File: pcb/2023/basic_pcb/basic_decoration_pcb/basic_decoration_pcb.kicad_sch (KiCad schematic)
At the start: 15 parts, among them J1 Conn_01x15_Socket, J2 Conn_01x15_Socket, J3 Screw_Terminal_01x03, Q1 BT136-500, U1 MOC3041M

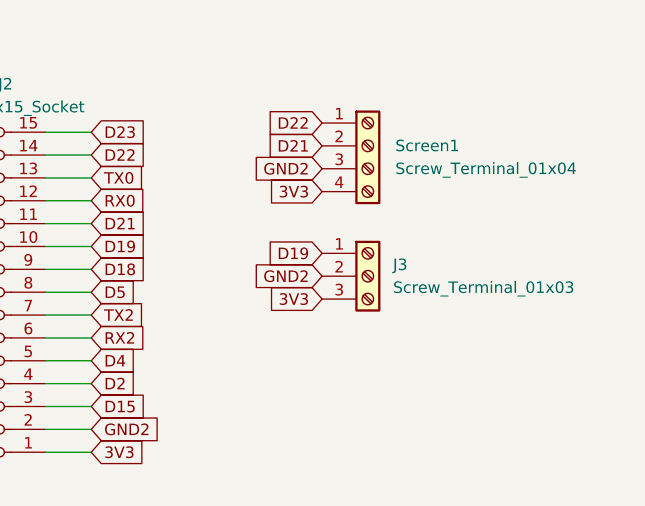
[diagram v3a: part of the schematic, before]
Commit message: update, fixed bug on the PCB, a pull up resistor is required for the DHT11 to work well, so now it's added
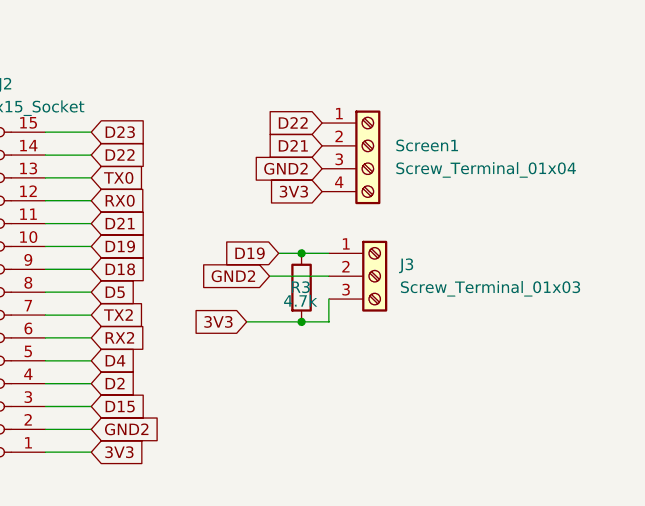
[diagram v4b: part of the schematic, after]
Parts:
- added R3: 4.7k_0603, Resistor_THT:R_Axial_DIN0204_L3.6mm_D1.6mm_P7.62mm_Horizontal, symbol PCM_4ms_Resistor:4.7k_0603
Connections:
- net 3V3: now also R3.2
- net D19: now also R3.1
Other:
- moved on the sheet: J3
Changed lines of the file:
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@@
 (kicad_sch (version 20230121) (generator eeschema)
   (paper "A4")
+  (junction (at 149.86 75.692) (diameter 0) (color 0 0 0 0)
+  )
   (junction (at 39.116 69.342) (diameter 0) (color 0 0 0 0)
   )
+  (junction (at 149.86 83.312) (diameter 0) (color 0 0 0 0)
+  )
   (wire (pts (xy 121.412 64.77) (xy 126.492 64.77))
     (stroke (width 0) (type default))
@@
     (stroke (width 0) (type default))
   )
+  (wire (pts (xy 149.86 75.692) (xy 152.908 75.692))
+    (stroke (width 0) (type default))
+  )
   (wire (pts (xy 37.846 40.64) (xy 37.846 42.672))
     (stroke (width 0) (type default))
@@
     (stroke (width 0) (type default))
   )
+  (wire (pts (xy 147.32 75.692) (xy 149.86 75.692))
+    (stroke (width 0) (type default))
+  )
   (polyline (pts (xy 94.742 27.432) (xy 124.714 27.432))
     (stroke (width 0) (type default))
@@
     (stroke (width 0) (type default))
   )
+  (wire (pts (xy 152.908 78.232) (xy 146.304 78.232))
+    (stroke (width 0) (type default))
+  )
   (wire (pts (xy 82.042 64.77) (xy 88.392 64.77))
     (stroke (width 0) (type default))
@@
     (stroke (width 0) (type default))
   )
+  (wire (pts (xy 149.86 83.312) (xy 152.908 83.312))
+    (stroke (width 0) (type default))
+  )
   (wire (pts (xy 121.412 92.71) (xy 126.492 92.71))
     (stroke (width 0) (type default))
@@
     (stroke (width 0) (type default))
   )
+  (wire (pts (xy 143.764 83.312) (xy 149.86 83.312))
+    (stroke (width 0) (type default))
+  )
   (polyline (pts (xy 124.714 27.432) (xy 124.714 47.498))
+    (stroke (width 0) (type default))
+  )
+  (wire (pts (xy 152.908 83.312) (xy 152.908 80.772))
     (stroke (width 0) (type default))
   )
@@
     )
   )
-  (global_label "GND2" (shape input) (at 152.146 78.232 180) (fields_autoplaced)
-    (effects (font (size 1.27 1.27)) (justify right))
-    (property "Intersheetrefs" "${INTERSHEET_REFS}" (at 144.0808 78.232 0)
+  (global_label "GND2" (shape input) (at 146.304 78.232 180) (fields_autoplaced)
+    (effects (font (size 1.27 1.27)) (justify right))
+    (property "Intersheetrefs" "${INTERSHEET_REFS}" (at 138.2388 78.232 0)
       (effects (font (size 1.27 1.27)) (justify right) hide)
     )
@@
     )
   )
-  (global_label "3V3" (shape input) (at 152.146 80.772 180) (fields_autoplaced)
-    (effects (font (size 1.27 1.27)) (justify right))
-    (property "Intersheetrefs" "${INTERSHEET_REFS}" (at 145.6532 80.772 0)
+  (global_label "3V3" (shape input) (at 143.764 83.312 180) (fields_autoplaced)
+    (effects (font (size 1.27 1.27)) (justify right))
+    (property "Intersheetrefs" "${INTERSHEET_REFS}" (at 137.2712 83.312 0)
       (effects (font (size 1.27 1.27)) (justify right) hide)
     )
@@
     )
   )
-  (global_label "D19" (shape input) (at 152.146 75.692 180) (fields_autoplaced)
-    (effects (font (size 1.27 1.27)) (justify right))
-    (property "Intersheetrefs" "${INTERSHEET_REFS}" (at 145.5512 75.692 0)
+  (global_label "D19" (shape input) (at 147.32 75.692 180) (fields_autoplaced)
+    (effects (font (size 1.27 1.27)) (justify right))
+    (property "Intersheetrefs" "${INTERSHEET_REFS}" (at 140.7252 75.692 0)
       (effects (font (size 1.27 1.27)) (justify right) hide)
     )
@@
     )
   )
-  (symbol (lib_id "Connector:Screw_Terminal_01x03") (at 157.226 78.232 0) (unit 1)
+  (symbol (lib_id "Connector:Screw_Terminal_01x03") (at 157.988 78.232 0) (unit 1)
     (in_bom yes) (on_board yes) (dnp no) (fields_autoplaced)
-    (property "Reference" "J3" (at 160.02 76.962 0)
-      (effects (font (size 1.27 1.27)) (justify left))
-    )
-    (property "Value" "Screw_Terminal_01x03" (at 160.02 79.502 0)
-      (effects (font (size 1.27 1.27)) (justify left))
-    )
-    (property "Footprint" "TerminalBlock:TerminalBlock_Altech_AK300-3_P5.00mm" (at 157.226 78.232 0)
-      (effects (font (size 1.27 1.27)) hide)
-    )
-    (property "Datasheet" "~" (at 157.226 78.232 0)
+    (property "Reference" "J3" (at 160.782 76.962 0)
+      (effects (font (size 1.27 1.27)) (justify left))
+    )
+    (property "Value" "Screw_Terminal_01x03" (at 160.782 79.502 0)
+      (effects (font (size 1.27 1.27)) (justify left))
+    )
+    (property "Footprint" "TerminalBlock:TerminalBlock_Altech_AK300-3_P5.00mm" (at 157.988 78.232 0)
+      (effects (font (size 1.27 1.27)) hide)
+    )
+    (property "Datasheet" "~" (at 157.988 78.232 0)
       (effects (font (size 1.27 1.27)) hide)
     )
@@
         )
       )
+    )
+  )
+  (symbol (lib_id "PCM_4ms_Resistor:4.7k_0603") (at 149.86 79.502 0) (unit 1)
+    (in_bom yes) (on_board yes) (dnp no)
+    (property "Reference" "R3" (at 148.59 79.502 0)
+      (effects (font (size 1.27 1.27)) (justify left))
+    )
+    (property "Value" "4.7k_0603" (at 147.32 79.502 90)
+      (effects (font (size 1.27 1.27)) hide)
+    )
+    (property "Footprint" "Resistor_THT:R_Axial_DIN0204_L3.6mm_D1.6mm_P7.62mm_Horizontal" (at 147.32 92.202 0)
+      (effects (font (size 1.27 1.27)) (justify left) hide)
+    )
+    (property "Datasheet" "" (at 149.86 79.502 0)
+      (effects (font (size 1.27 1.27)) hide)
+    )
+    (property "Specifications" "4k7, 1%, 1/10W, 0603" (at 147.32 87.376 0)
+      (effects (font (size 1.27 1.27)) (justify left) hide)
+    )
+    (property "Manufacturer" "Yageo" (at 147.32 88.9 0)
+      (effects (font (size 1.27 1.27)) (justify left) hide)
+    )
+    (property "Part Number" "RC0603FR-074K7L" (at 147.32 90.424 0)
+      (effects (font (size 1.27 1.27)) (justify left) hide)
+    )
+    (property "Display" "4.7k" (at 147.828 81.026 0)
+      (effects (font (size 1.27 1.27)) (justify left))
+    )
+    (property "JLCPCB ID" "C23162" (at 149.86 79.502 0)
+      (effects (font (size 1.27 1.27)) hide)
+    )
+    (pin "1")
+    (pin "2")
+    (instances
+      (project "basic_decoration_pcb"
+        (path "/e2e9caae-b3c7-4a5d-81db-191a274f7dfe"
+          (reference "R3") (unit 1)
+        )
+      )
